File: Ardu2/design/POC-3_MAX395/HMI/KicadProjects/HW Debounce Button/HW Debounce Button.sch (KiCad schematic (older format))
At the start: 4 parts

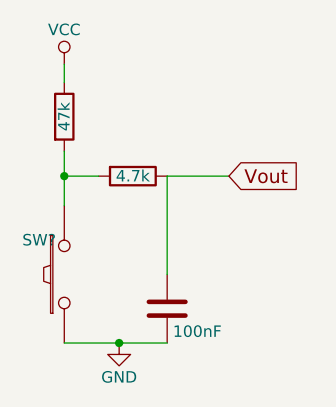
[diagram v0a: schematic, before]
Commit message: trying to get HW debouncing to work with interrupts
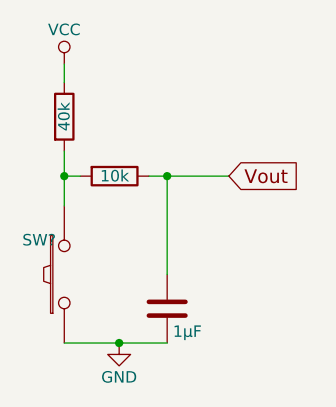
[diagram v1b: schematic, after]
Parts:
- C?: value 100nF -> 1µF
- R?: value 47k -> 40k
- R?: value 4.7k -> 10k
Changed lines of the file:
@@
 LIBS:contrib
 LIBS:valves
+LIBS:HW Debounce Button-cache
 EELAYER 25 0
 EELAYER END
@@
 P 3500 2290
 F 0 "R?" V 3580 2290 50  0001 C CNN
-F 1 "47k" V 3500 2290 50  0000 C CNN
+F 1 "40k" V 3500 2290 50  0000 C CNN
 F 2 "" V 3430 2290 50  0000 C CNN
 F 3 "" H 3500 2290 50  0000 C CNN
@@
 L R R?
 U 1 1 566DB317
-P 3800 2550
-F 0 "R?" V 3880 2550 50  0001 C CNN
-F 1 "4.7k" V 3800 2550 50  0000 C CNN
-F 2 "" V 3730 2550 50  0000 C CNN
-F 3 "" H 3800 2550 50  0000 C CNN
-	1    3800 2550
+P 3720 2550
+F 0 "R?" V 3800 2550 50  0001 C CNN
+F 1 "10k" V 3720 2550 50  0000 C CNN
+F 2 "" V 3650 2550 50  0000 C CNN
+F 3 "" H 3720 2550 50  0000 C CNN
+	1    3720 2550
 	0    1    1    0
 $EndComp
@@
 P 3950 3130
 F 0 "C?" H 3975 3230 50  0001 L CNN
-F 1 "100nF" H 3975 3030 50  0000 L CNN
+F 1 "1µF" H 3975 3030 50  0000 L CNN
 F 2 "" H 3988 2980 50  0000 C CNN
 F 3 "" H 3950 3130 50  0000 C CNN
@@
 $EndComp
 Wire Wire Line
-	3500 2440 3500 2680
+	3500 2440 3500 2550
 Wire Wire Line
-	3650 2550 3500 2550
+	3500 2550 3500 2680
+Wire Wire Line
+	3570 2550 3500 2550
 Connection ~ 3500 2550
 Wire Wire Line
-	3950 2550 3950 2980
+	3500 3280 3740 3280
 Wire Wire Line
-	3500 3280 3950 3280
+	3740 3280 3950 3280
 Connection ~ 3740 3280
+Wire Wire Line
+	3870 2550 3950 2550
 Wire Wire Line
 	3950 2550 4220 2550
@@
 Wire Wire Line
 	3500 2060 3500 2140
+Wire Wire Line
+	3950 2980 3950 2550
+Connection ~ 3950 2550
 $EndSCHEMATC

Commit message: HW debounce update
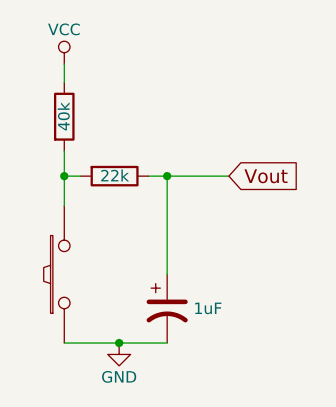
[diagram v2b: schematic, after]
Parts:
- removed C?: 1µF, symbol C
- added C1: 1uF, symbol CP1
- R2: renamed from R?; value 10k -> 22k
- gave numbers to parts that had none: 2
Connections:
- net GND: now also C1.2
- net Vout: now also C1.1
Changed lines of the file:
@@
 $EndDescr
 $Comp
-L SW_PUSH SW?
+L SW_PUSH SW1
 U 1 1 566DB135
 P 3500 2980
-F 0 "SW?" V 3650 3090 50  0000 C CNN
+F 0 "SW1" V 3650 3090 50  0001 C CNN
 F 1 "SW_PUSH" V 3500 2900 50  0001 C CNN
 F 2 "" H 3500 2980 50  0000 C CNN
@@
 $EndComp
 $Comp
-L GND #PWR?
+L GND #PWR01
 U 1 1 566DB239
 P 3740 3280
-F 0 "#PWR?" H 3740 3030 50  0001 C CNN
+F 0 "#PWR01" H 3740 3030 50  0001 C CNN
 F 1 "GND" H 3740 3130 50  0000 C CNN
 F 2 "" H 3740 3280 50  0000 C CNN
@@
 $EndComp
 $Comp
-L VCC #PWR?
+L VCC #PWR02
 U 1 1 566DB25A
 P 3500 2060
-F 0 "#PWR?" H 3500 1910 50  0001 C CNN
+F 0 "#PWR02" H 3500 1910 50  0001 C CNN
 F 1 "VCC" H 3500 2210 50  0000 C CNN
 F 2 "" H 3500 2060 50  0000 C CNN
@@
 $EndComp
 $Comp
-L R R?
+L R R1
 U 1 1 566DB278
 P 3500 2290
-F 0 "R?" V 3580 2290 50  0001 C CNN
+F 0 "R1" V 3580 2290 50  0001 C CNN
 F 1 "40k" V 3500 2290 50  0000 C CNN
 F 2 "" V 3430 2290 50  0000 C CNN
@@
 $EndComp
 $Comp
-L R R?
+L R R2
 U 1 1 566DB317
 P 3720 2550
-F 0 "R?" V 3800 2550 50  0001 C CNN
-F 1 "10k" V 3720 2550 50  0000 C CNN
+F 0 "R2" V 3800 2550 50  0001 C CNN
+F 1 "22k" V 3720 2550 50  0000 C CNN
 F 2 "" V 3650 2550 50  0000 C CNN
 F 3 "" H 3720 2550 50  0000 C CNN
@@
 	0    1    1    0
 $EndComp
-$Comp
-L C C?
-U 1 1 566DB36E
-P 3950 3130
-F 0 "C?" H 3975 3230 50  0001 L CNN
-F 1 "1µF" H 3975 3030 50  0000 L CNN
-F 2 "" H 3988 2980 50  0000 C CNN
-F 3 "" H 3950 3130 50  0000 C CNN
-	1    3950 3130
-	1    0    0    -1
-$EndComp
 Wire Wire Line
-	3500 2440 3500 2550
-Wire Wire Line
-	3500 2550 3500 2680
+	3500 2440 3500 2680
 Wire Wire Line
 	3570 2550 3500 2550
 Connection ~ 3500 2550
 Wire Wire Line
-	3500 3280 3740 3280
-Wire Wire Line
-	3740 3280 3950 3280
+	3500 3280 3950 3280
 Connection ~ 3740 3280
 Wire Wire Line
-	3870 2550 3950 2550
-Wire Wire Line
-	3950 2550 4220 2550
+	3870 2550 4220 2550
 Text GLabel 4220 2550 2    60   Input ~ 0
 Vout
@@
 	3950 2980 3950 2550
 Connection ~ 3950 2550
+$Comp
+L CP1 C1
+U 1 1 5675BF29
+P 3950 3130
+F 0 "C1" H 4065 3176 50  0001 L CNN
+F 1 "1uF" H 4065 3130 50  0000 L CNN
+F 2 "" H 3950 3130 50  0000 C CNN
+F 3 "" H 3950 3130 50  0000 C CNN
+	1    3950 3130
+	1    0    0    -1
+$EndComp
 $EndSCHEMATC

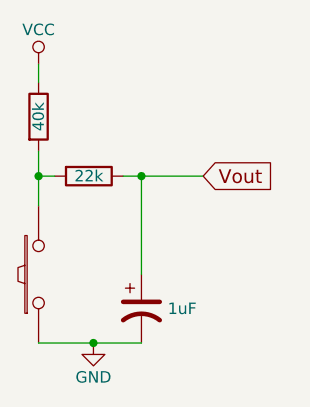
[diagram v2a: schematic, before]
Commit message: more hw debouncing, seems a bit better
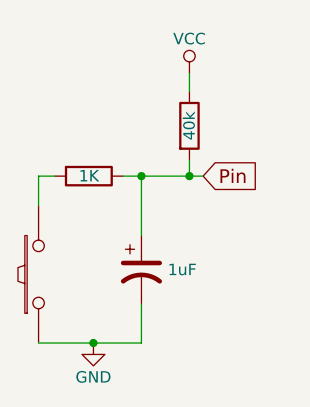
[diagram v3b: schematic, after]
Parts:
- R2: value 22k -> 1K
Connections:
- net at R2.2, SW1.2: no longer R1.2
- net Vout renamed Pin
- net Pin: now also R1.2
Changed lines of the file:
@@
 L VCC #PWR02
 U 1 1 566DB25A
-P 3500 2060
-F 0 "#PWR02" H 3500 1910 50  0001 C CNN
-F 1 "VCC" H 3500 2210 50  0000 C CNN
-F 2 "" H 3500 2060 50  0000 C CNN
-F 3 "" H 3500 2060 50  0000 C CNN
-	1    3500 2060
+P 4160 2100
+F 0 "#PWR02" H 4160 1950 50  0001 C CNN
+F 1 "VCC" H 4160 2250 50  0000 C CNN
+F 2 "" H 4160 2100 50  0000 C CNN
+F 3 "" H 4160 2100 50  0000 C CNN
+	1    4160 2100
 	1    0    0    -1
 $EndComp
@@
 L R R1
 U 1 1 566DB278
-P 3500 2290
-F 0 "R1" V 3580 2290 50  0001 C CNN
-F 1 "40k" V 3500 2290 50  0000 C CNN
-F 2 "" V 3430 2290 50  0000 C CNN
-F 3 "" H 3500 2290 50  0000 C CNN
-	1    3500 2290
+P 4160 2330
+F 0 "R1" V 4240 2330 50  0001 C CNN
+F 1 "40k" V 4160 2330 50  0000 C CNN
+F 2 "" V 4090 2330 50  0000 C CNN
+F 3 "" H 4160 2330 50  0000 C CNN
+	1    4160 2330
 	1    0    0    -1
 $EndComp
@@
 P 3720 2550
 F 0 "R2" V 3800 2550 50  0001 C CNN
-F 1 "22k" V 3720 2550 50  0000 C CNN
+F 1 "1K" V 3720 2550 50  0000 C CNN
 F 2 "" V 3650 2550 50  0000 C CNN
 F 3 "" H 3720 2550 50  0000 C CNN
@@
 $EndComp
 Wire Wire Line
-	3500 2440 3500 2680
-Wire Wire Line
-	3570 2550 3500 2550
-Connection ~ 3500 2550
+	3500 2550 3570 2550
 Wire Wire Line
 	3500 3280 3950 3280
@@
 	3870 2550 4220 2550
 Text GLabel 4220 2550 2    60   Input ~ 0
-Vout
+Pin
 Wire Wire Line
-	3500 2060 3500 2140
-Wire Wire Line
-	3950 2980 3950 2550
+	3950 2810 3950 2550
 Connection ~ 3950 2550
 $Comp
 L CP1 C1
 U 1 1 5675BF29
-P 3950 3130
-F 0 "C1" H 4065 3176 50  0001 L CNN
-F 1 "1uF" H 4065 3130 50  0000 L CNN
-F 2 "" H 3950 3130 50  0000 C CNN
-F 3 "" H 3950 3130 50  0000 C CNN
-	1    3950 3130
+P 3950 2960
+F 0 "C1" H 4065 3006 50  0001 L CNN
+F 1 "1uF" H 4065 2960 50  0000 L CNN
+F 2 "" H 3950 2960 50  0000 C CNN
+F 3 "" H 3950 2960 50  0000 C CNN
+	1    3950 2960
 	1    0    0    -1
 $EndComp
+Wire Wire Line
+	4160 2100 4160 2180
+Wire Wire Line
+	4160 2480 4160 2550
+Connection ~ 4160 2550
+Wire Wire Line
+	3500 2550 3500 2680
+Wire Wire Line
+	3950 3280 3950 3110
 $EndSCHEMATC

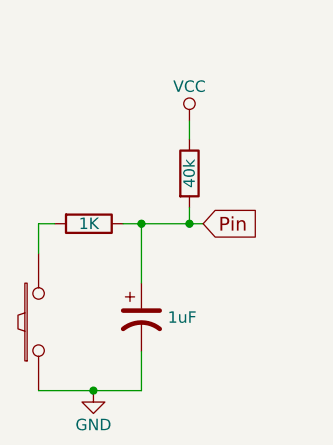
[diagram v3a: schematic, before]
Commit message: hw debouncing now works, circuit is updated, code remains the same.
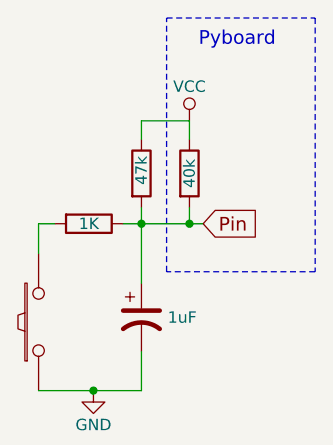
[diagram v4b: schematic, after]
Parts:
- added R?: 47k, symbol R
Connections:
- net Pin: now also R?.2
- net VCC: now also R?.1
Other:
- note added: "Pyboard"
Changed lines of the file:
@@
 Pin
 Wire Wire Line
-	3950 2810 3950 2550
+	3950 2480 3950 2810
 Connection ~ 3950 2550
 $Comp
@@
 Wire Wire Line
 	3950 3280 3950 3110
+$Comp
+L R R?
+U 1 1 56929606
+P 3950 2330
+F 0 "R?" H 4020 2376 50  0001 L CNN
+F 1 "47k" V 3950 2280 50  0000 L CNN
+F 2 "" V 3880 2330 50  0000 C CNN
+F 3 "" H 3950 2330 50  0000 C CNN
+	1    3950 2330
+	1    0    0    -1
+$EndComp
+Wire Wire Line
+	3950 2180 3950 2100
+Wire Wire Line
+	3950 2100 4160 2100
+Wire Notes Line
+	4060 2760 4060 1650
+Wire Notes Line
+	4060 1650 4710 1650
+Wire Notes Line
+	4710 1650 4710 2760
+Wire Notes Line
+	4710 2760 4060 2760
+Text Notes 4200 1780 0    60   ~ 0
+Pyboard
 $EndSCHEMATC

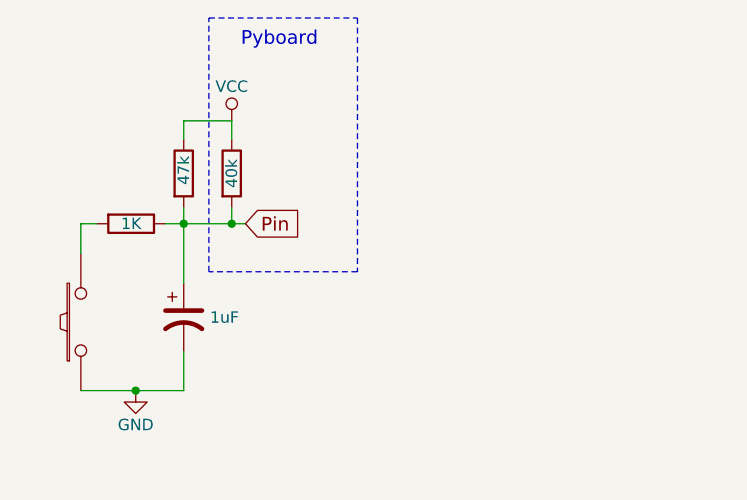
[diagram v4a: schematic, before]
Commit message: working on debounce hmi pcb and panel
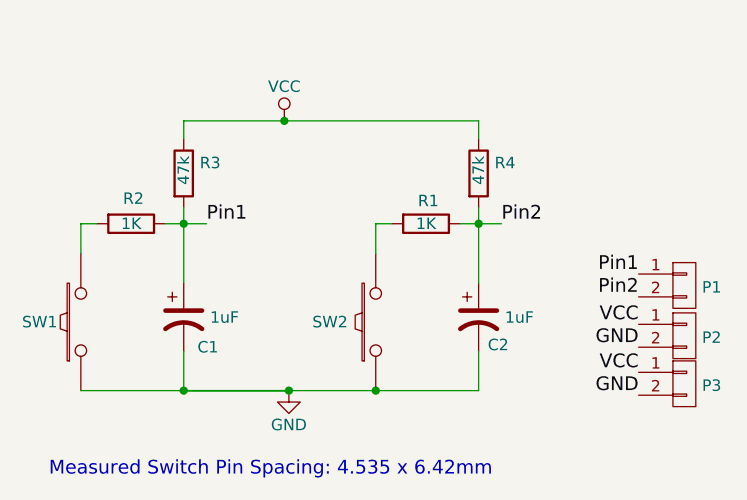
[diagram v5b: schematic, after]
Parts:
- added C2: 1uF, Capacitors_ThroughHole:C_Radial_D5_L11_P2, symbol CP1
- added P1, P2, P3: CONN_01X02, Pin_Headers:Pin_Header_Straight_1x02, symbol CONN_01X02
- added R4: 47k, Resistors_ThroughHole:Resistor_Horizontal_RM10mm, symbol R
- added SW2: SW_PUSH, misc:AB2_PB_MOM_6MM_PTH_BLK, symbol SW_PUSH
- C1: footprint (none) -> Capacitors_ThroughHole:C_Radial_D5_L11_P2
- R1: value 40k -> 1K; footprint (none) -> Resistors_ThroughHole:Resistor_Horizontal_RM10mm
- R2: footprint (none) -> Resistors_ThroughHole:Resistor_Horizontal_RM10mm
- R3: renamed from R?; footprint (none) -> Resistors_ThroughHole:Resistor_Horizontal_RM10mm
- SW1: footprint (none) -> misc:AB2_PB_MOM_6MM_PTH_BLK
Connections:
- net GND: now also C2.2, P2.2 (P2), P3.2 (P2), SW2.1
- net VCC: now also P2.1 (P1), P3.1 (P1), R4.1; no longer R1.1
- net Pin renamed Pin1
- net Pin1: now also P1.1 (P1); no longer R1.2
- new net: R1.2, SW2.2
- new net Pin2: C2.1, P1.2 (P2), R1.1, R4.2
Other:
- note added: "Measured Switch Pin Spacing: 4.535 x 6.42mm"
- note removed: "Pyboard"
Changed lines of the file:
@@
 U 1 1 566DB135
 P 3500 2980
-F 0 "SW1" V 3650 3090 50  0001 C CNN
+F 0 "SW1" V 3500 3160 50  0000 C CNN
 F 1 "SW_PUSH" V 3500 2900 50  0001 C CNN
-F 2 "" H 3500 2980 50  0000 C CNN
+F 2 "misc:AB2_PB_MOM_6MM_PTH_BLK" H 3500 2980 50  0001 C CNN
 F 3 "" H 3500 2980 50  0000 C CNN
 	1    3500 2980
@@
 L GND #PWR01
 U 1 1 566DB239
-P 3740 3280
-F 0 "#PWR01" H 3740 3030 50  0001 C CNN
-F 1 "GND" H 3740 3130 50  0000 C CNN
-F 2 "" H 3740 3280 50  0000 C CNN
-F 3 "" H 3740 3280 50  0000 C CNN
-	1    3740 3280
+P 4410 3280
+F 0 "#PWR01" H 4410 3030 50  0001 C CNN
+F 1 "GND" H 4410 3130 50  0000 C CNN
+F 2 "" H 4410 3280 50  0000 C CNN
+F 3 "" H 4410 3280 50  0000 C CNN
+	1    4410 3280
 	1    0    0    -1
 $EndComp
@@
 L VCC #PWR02
 U 1 1 566DB25A
-P 4160 2100
-F 0 "#PWR02" H 4160 1950 50  0001 C CNN
-F 1 "VCC" H 4160 2250 50  0000 C CNN
-F 2 "" H 4160 2100 50  0000 C CNN
-F 3 "" H 4160 2100 50  0000 C CNN
-	1    4160 2100
-	1    0    0    -1
-$EndComp
-$Comp
-L R R1
-U 1 1 566DB278
-P 4160 2330
-F 0 "R1" V 4240 2330 50  0001 C CNN
-F 1 "40k" V 4160 2330 50  0000 C CNN
-F 2 "" V 4090 2330 50  0000 C CNN
-F 3 "" H 4160 2330 50  0000 C CNN
-	1    4160 2330
+P 4390 2100
+F 0 "#PWR02" H 4390 1950 50  0001 C CNN
+F 1 "VCC" H 4390 2250 50  0000 C CNN
+F 2 "" H 4390 2100 50  0000 C CNN
+F 3 "" H 4390 2100 50  0000 C CNN
+	1    4390 2100
 	1    0    0    -1
 $EndComp
@@
 U 1 1 566DB317
 P 3720 2550
-F 0 "R2" V 3800 2550 50  0001 C CNN
+F 0 "R2" V 3610 2560 50  0000 C CNN
 F 1 "1K" V 3720 2550 50  0000 C CNN
-F 2 "" V 3650 2550 50  0000 C CNN
+F 2 "Resistors_ThroughHole:Resistor_Horizontal_RM10mm" V 3650 2550 50  0001 C CNN
 F 3 "" H 3720 2550 50  0000 C CNN
 	1    3720 2550
@@
 Wire Wire Line
 	3500 3280 3950 3280
-Connection ~ 3740 3280
-Wire Wire Line
-	3870 2550 4220 2550
-Text GLabel 4220 2550 2    60   Input ~ 0
-Pin
-Wire Wire Line
-	3950 2480 3950 2810
+Wire Wire Line
+	3950 3280 4410 3280
+Wire Wire Line
+	4410 3280 3950 3280
+Wire Wire Line
+	3950 3280 4410 3280
+Wire Wire Line
+	4410 3280 4790 3280
+Wire Wire Line
+	4790 3280 5240 3280
+Connection ~ 4410 3280
+Wire Wire Line
+	3950 2480 3950 2550
+Wire Wire Line
+	3950 2550 3950 2810
 Connection ~ 3950 2550
 $Comp
@@
 U 1 1 5675BF29
 P 3950 2960
-F 0 "C1" H 4065 3006 50  0001 L CNN
+F 0 "C1" H 4010 2830 50  0000 L CNN
 F 1 "1uF" H 4065 2960 50  0000 L CNN
-F 2 "" H 3950 2960 50  0000 C CNN
+F 2 "Capacitors_ThroughHole:C_Radial_D5_L11_P2" H 3950 2960 50  0001 C CNN
 F 3 "" H 3950 2960 50  0000 C CNN
 	1    3950 2960
@@
 $EndComp
 Wire Wire Line
-	4160 2100 4160 2180
-Wire Wire Line
-	4160 2480 4160 2550
-Connection ~ 4160 2550
-Wire Wire Line
 	3500 2550 3500 2680
 Wire Wire Line
 	3950 3280 3950 3110
 $Comp
-L R R?
+L R R3
 U 1 1 56929606
 P 3950 2330
-F 0 "R?" H 4020 2376 50  0001 L CNN
+F 0 "R3" H 4020 2376 50  0000 L CNN
 F 1 "47k" V 3950 2280 50  0000 L CNN
-F 2 "" V 3880 2330 50  0000 C CNN
+F 2 "Resistors_ThroughHole:Resistor_Horizontal_RM10mm" V 3880 2330 50  0001 C CNN
 F 3 "" H 3950 2330 50  0000 C CNN
 	1    3950 2330
@@
 	3950 2180 3950 2100
 Wire Wire Line
-	3950 2100 4160 2100
-Wire Notes Line
-	4060 2760 4060 1650
-Wire Notes Line
-	4060 1650 4710 1650
-Wire Notes Line
-	4710 1650 4710 2760
-Wire Notes Line
-	4710 2760 4060 2760
-Text Notes 4200 1780 0    60   ~ 0
-Pyboard
+	3950 2100 4390 2100
+Wire Wire Line
+	4390 2100 5240 2100
+Text Notes 3360 3660 0    60   ~ 0
+Measured Switch Pin Spacing: 4.535 x 6.42mm
+Wire Wire Line
+	3870 2550 3950 2550
+Wire Wire Line
+	3950 2550 4050 2550
+Text Label 4050 2550 0    60   ~ 0
+Pin1
+$Comp
+L SW_PUSH SW2
+U 1 1 56A4BAC7
+P 4790 2980
+F 0 "SW2" V 4790 3180 50  0000 C CNN
+F 1 "SW_PUSH" V 4790 2900 50  0001 C CNN
+F 2 "misc:AB2_PB_MOM_6MM_PTH_BLK" H 4790 2980 50  0001 C CNN
+F 3 "" H 4790 2980 50  0000 C CNN
+	1    4790 2980
+	0    -1   -1   0
+$EndComp
+$Comp
+L R R1
+U 1 1 56A4BAD3
+P 5010 2550
+F 0 "R1" V 4910 2560 50  0000 C CNN
+F 1 "1K" V 5010 2550 50  0000 C CNN
+F 2 "Resistors_ThroughHole:Resistor_Horizontal_RM10mm" V 4940 2550 50  0001 C CNN
+F 3 "" H 5010 2550 50  0000 C CNN
+	1    5010 2550
+	0    1    1    0
+$EndComp
+Wire Wire Line
+	4790 2550 4860 2550
+Wire Wire Line
+	5240 2480 5240 2550
+Wire Wire Line
+	5240 2550 5240 2810
+Connection ~ 5240 2550
+$Comp
+L CP1 C2
+U 1 1 56A4BADC
+P 5240 2960
+F 0 "C2" H 5280 2840 50  0000 L CNN
+F 1 "1uF" H 5355 2960 50  0000 L CNN
+F 2 "Capacitors_ThroughHole:C_Radial_D5_L11_P2" H 5240 2960 50  0001 C CNN
+F 3 "" H 5240 2960 50  0000 C CNN
+	1    5240 2960
+	1    0    0    -1
+$EndComp
+Wire Wire Line
+	4790 2550 4790 2680
+Wire Wire Line
+	5240 3280 5240 3110
+$Comp
+L R R4
+U 1 1 56A4BAE4
+P 5240 2330
+F 0 "R4" H 5310 2376 50  0000 L CNN
+F 1 "47k" V 5240 2280 50  0000 L CNN
+F 2 "Resistors_ThroughHole:Resistor_Horizontal_RM10mm" V 5170 2330 50  0001 C CNN
+F 3 "" H 5240 2330 50  0000 C CNN
+	1    5240 2330
+	1    0    0    -1
+$EndComp
+Wire Wire Line
+	5240 2100 5240 2180
+Wire Wire Line
+	5160 2550 5240 2550
+Wire Wire Line
+	5240 2550 5340 2550
+Text Label 5340 2550 0    60   ~ 0
+Pin2
+Connection ~ 3950 3280
+Connection ~ 4790 3280
+Connection ~ 4390 2100
+Text Label 5940 3090 2    60   ~ 0
+GND
+Text Label 5940 2990 2    60   ~ 0
+VCC
+Text Label 5940 2870 2    60   ~ 0
+Pin2
+Text Label 5940 2770 2    60   ~ 0
+Pin1
+$Comp
+L CONN_01X02 P2
+U 1 1 56A4C5E0
+P 6140 3040
+F 0 "P2" H 6217 3032 50  0000 L CNN
+F 1 "CONN_01X02" H 6217 2986 50  0001 L CNN
+F 2 "Pin_Headers:Pin_Header_Straight_1x02" H 6140 3040 50  0001 C CNN
+F 3 "" H 6140 3040 50  0000 C CNN
+	1    6140 3040
+	1    0    0    -1
+$EndComp
+$Comp
+L CONN_01X02 P3
+U 1 1 56A4C6E2
+P 6140 3250
+F 0 "P3" H 6217 3242 50  0000 L CNN
+F 1 "CONN_01X02" H 6217 3196 50  0001 L CNN
+F 2 "Pin_Headers:Pin_Header_Straight_1x02" H 6140 3250 50  0001 C CNN
+F 3 "" H 6140 3250 50  0000 C CNN
+	1    6140 3250
+	1    0    0    -1
+$EndComp
+Text Label 5940 3200 2    60   ~ 0
+VCC
+Text Label 5940 3300 2    60   ~ 0
+GND
+$Comp
+L CONN_01X02 P1
+U 1 1 56A4C82A
+P 6140 2820
+F 0 "P1" H 6217 2812 50  0000 L CNN
+F 1 "CONN_01X02" H 6217 2766 50  0001 L CNN
+F 2 "Pin_Headers:Pin_Header_Straight_1x02" H 6140 2820 50  0001 C CNN
+F 3 "" H 6140 2820 50  0000 C CNN
+	1    6140 2820
+	1    0    0    -1
+$EndComp
 $EndSCHEMATC
